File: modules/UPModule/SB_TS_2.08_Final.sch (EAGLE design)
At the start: 68 parts, among them IC1 MC34063AD, IC2 MCP1702-33, IC3 LPC922FDH, Q1 BC856, Q2 BCP52, Q4 ASFL, T1 BC848, T2 BC848

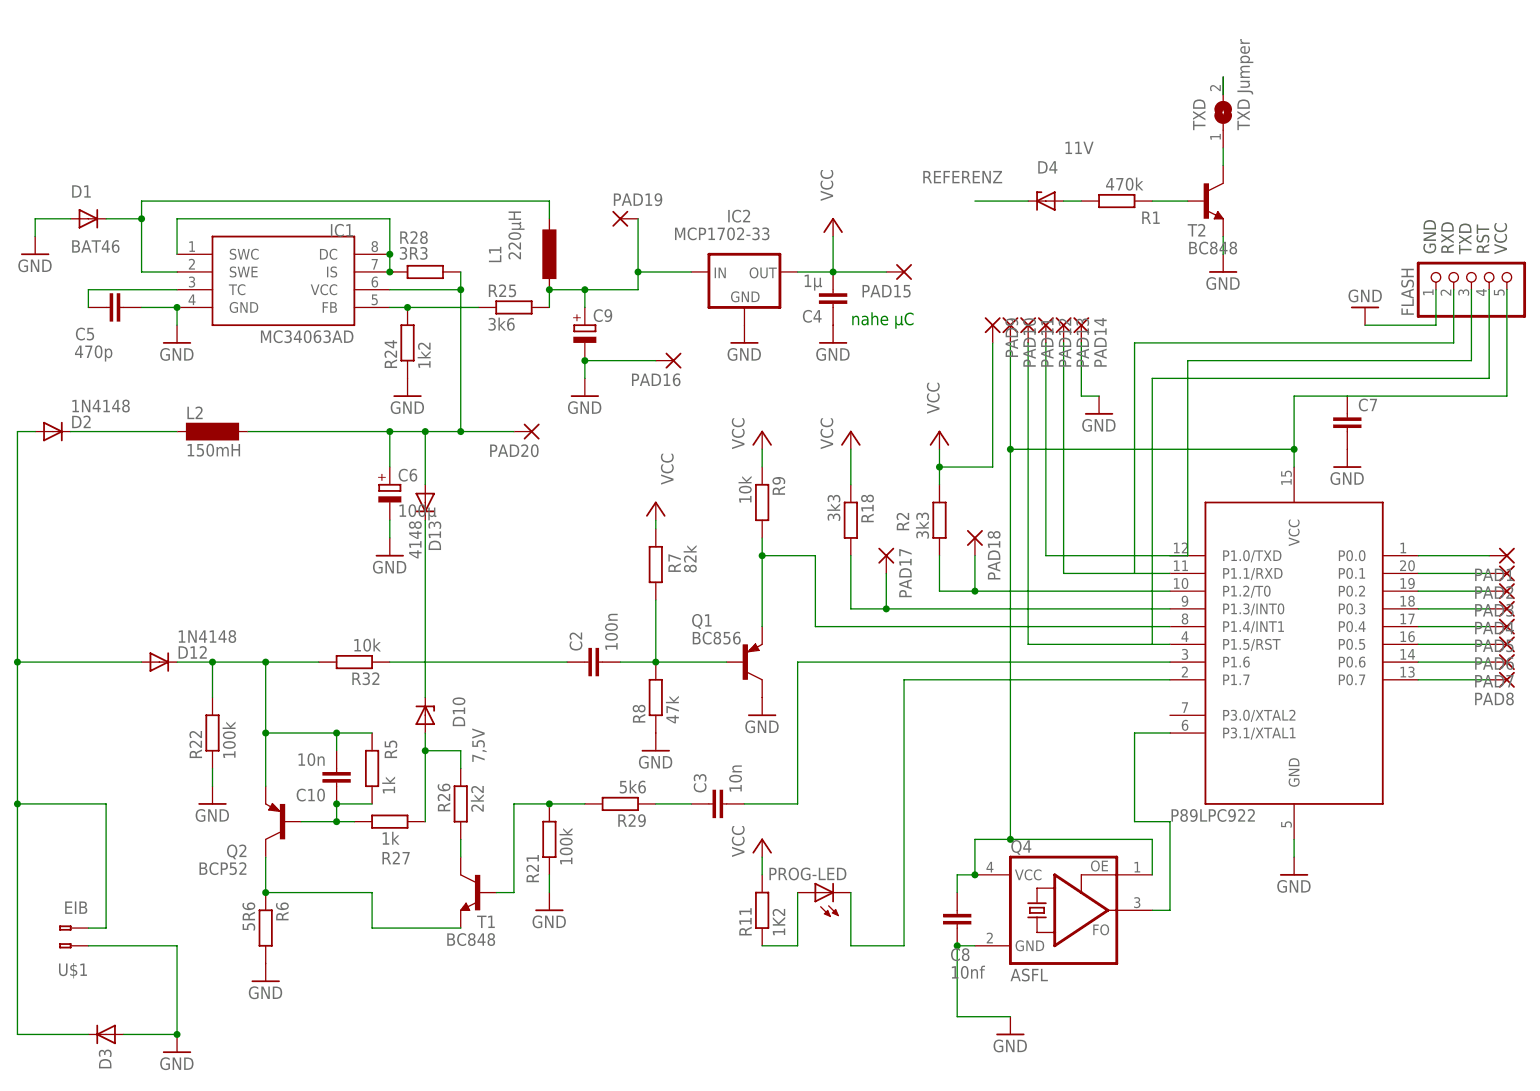
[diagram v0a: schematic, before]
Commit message: text placement optimized; missing values added
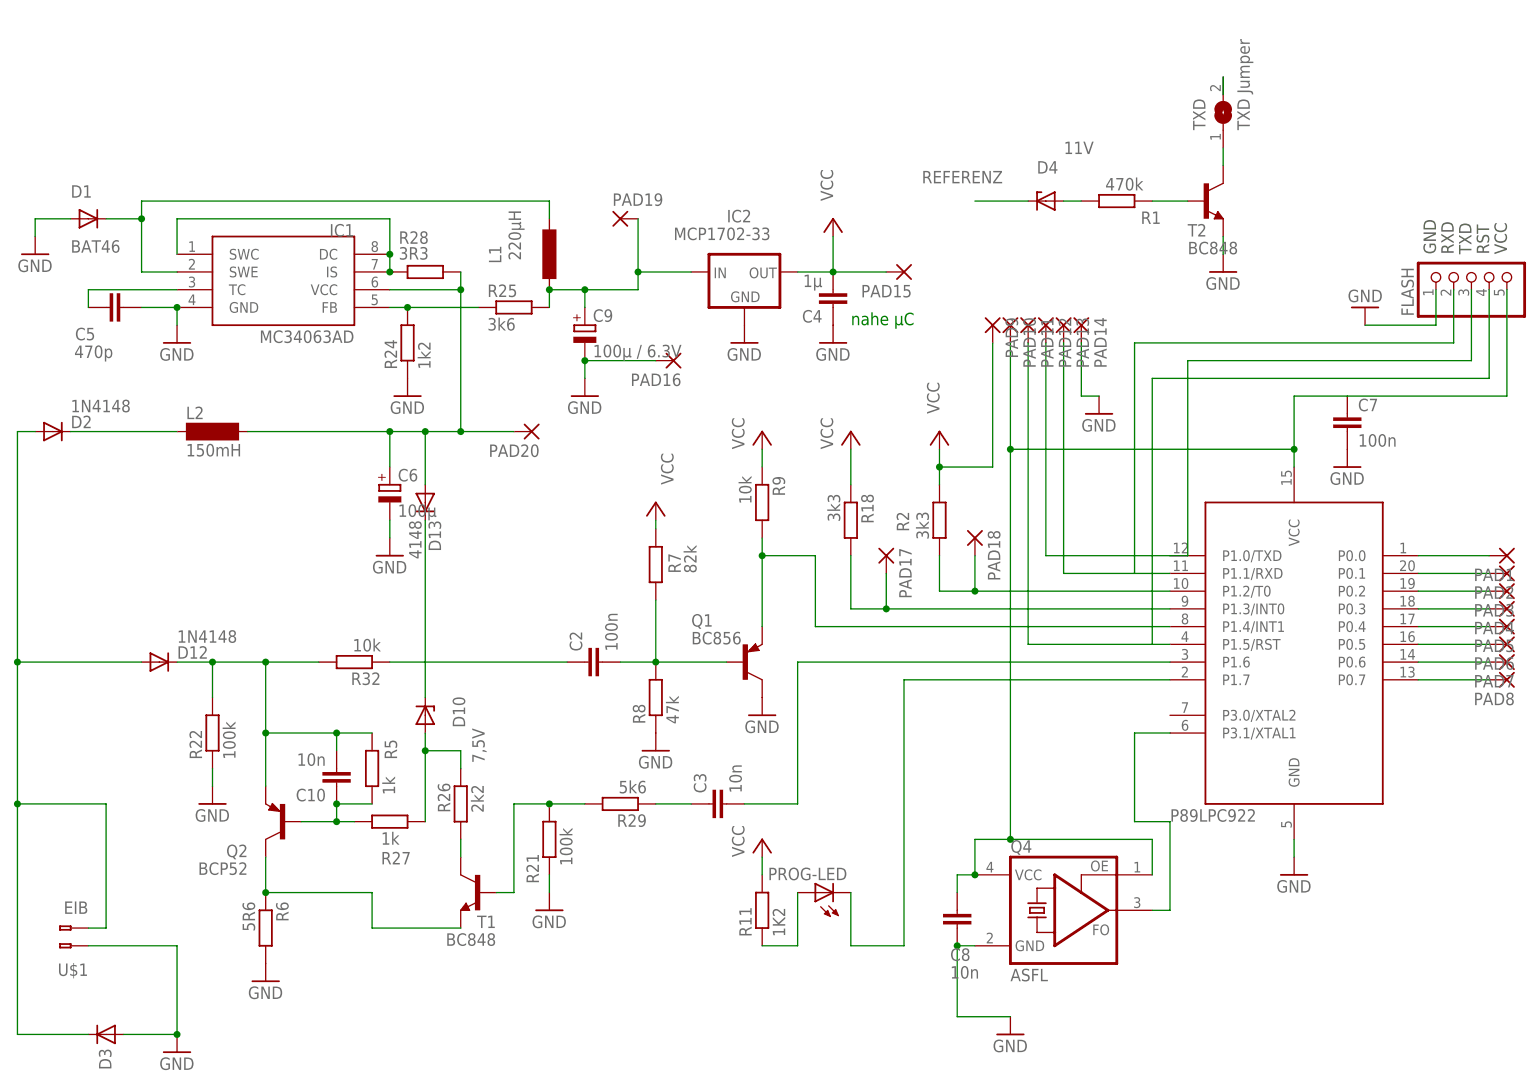
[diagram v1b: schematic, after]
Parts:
- C7: value (none) -> 100n
- C8: value 10nf -> 10n
- C9: value (none) -> 100µ / 6.3V
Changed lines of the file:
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@@
 <?xml version="1.0" encoding="utf-8"?>
 <!DOCTYPE eagle SYSTEM "eagle.dtd">
-<eagle version="6.5.0">
+<eagle version="8.5.0">
 <drawing>
 <settings>
 <setting alwaysvectorfont="no"/>
+<setting keepoldvectorfont="yes"/>
 <setting verticaltext="up"/>
 </settings>
@@
 <part name="P+5" library="supply1" deviceset="VCC" device=""/>
 <part name="R11" library="rcl" deviceset="R-EU_" device="R1206" value="1K2"/>
-<part name="C7" library="rcl" deviceset="C-EU" device="C1206"/>
-<part name="C8" library="rcl" deviceset="C-EU" device="C1206" value="10nf"/>
+<part name="C7" library="rcl" deviceset="C-EU" device="C1206" value="100n"/>
+<part name="C8" library="rcl" deviceset="C-EU" device="C1206" value="10n"/>
 <part name="Q4" library="crystal" deviceset="ASF*" device="" technology="L"/>
 <part name="R18" library="rcl" deviceset="R-EU_" device="R1206" value="3k3"/>
@@
 <part name="D1" library="diode" deviceset="DIODE-" device="MINIMELF" value="BAT46"/>
 <part name="R28" library="rcl" deviceset="R-EU_" device="M1206" value="3R3"/>
-<part name="C9" library="rcl" deviceset="CPOL-EU" device="E2.5-5"/>
+<part name="C9" library="rcl" deviceset="CPOL-EU" device="E2.5-5" value="100µ / 6.3V"/>
 <part name="D2" library="diode" deviceset="DIODE-" device="MINIMELF" value="1N4148"/>
 <part name="D3" library="semicon-smd-ipc" deviceset="D-" device="SMB" value="SMAJ40AC"/>
